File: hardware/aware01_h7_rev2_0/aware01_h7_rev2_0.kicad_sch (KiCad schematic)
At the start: 44 parts, among them J2 Conn_02x07_Odd_Even, J3 Conn_02x05_Odd_Even, SW1 SW_Push, U1 LMR50410Y5FQDBVRQ1, U2 STM32H7A3RITx, U7 LM1117MP-3.3, U8 LM4040DIM3X-10, Y2 WE-XTAL 24.0MHz 50ppm

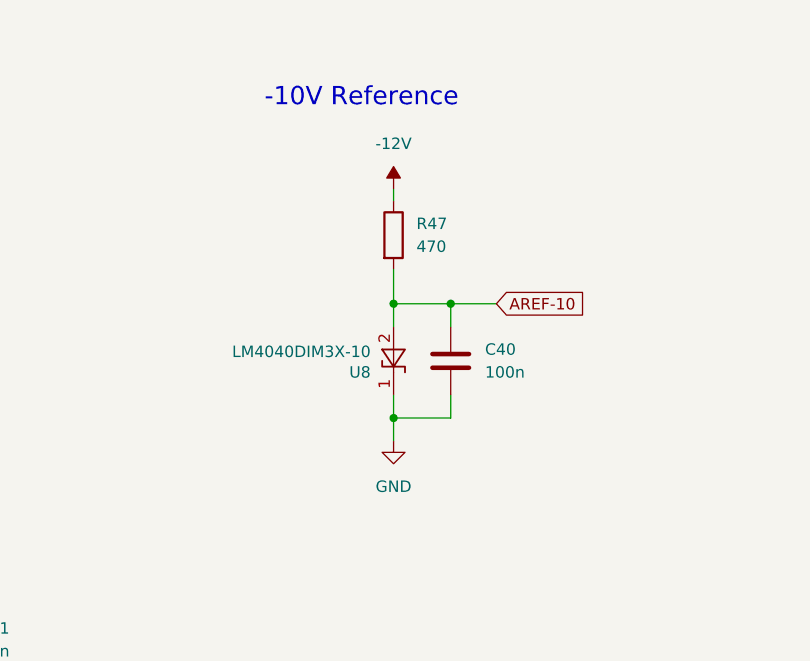
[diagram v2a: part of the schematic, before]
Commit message: refine layout, add testpoints
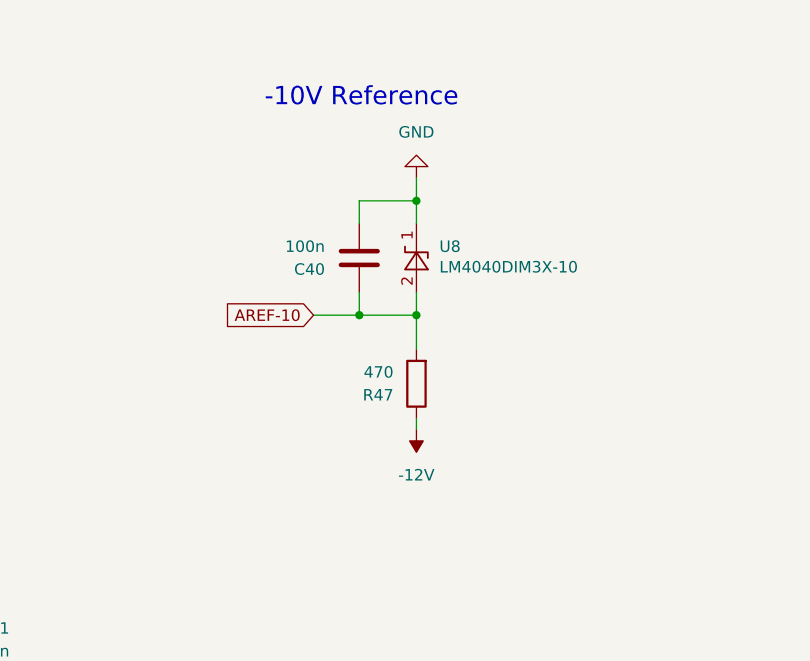
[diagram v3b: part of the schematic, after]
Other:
- moved on the sheet: C40, R47, U8
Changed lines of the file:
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@@
 	)
 	(junction
-		(at 274.32 57.15)
+		(at 276.86 58.42)
 		(diameter 0)
 		(color 0 0 0 0)
@@
 	)
 	(junction
-		(at 274.32 69.85)
+		(at 276.86 45.72)
 		(diameter 0)
 		(color 0 0 0 0)
@@
 	)
 	(junction
-		(at 280.67 57.15)
+		(at 270.51 58.42)
 		(diameter 0)
 		(color 0 0 0 0)
@@
 	(wire
 		(pts
-			(xy 274.32 44.45) (xy 274.32 45.72)
+			(xy 276.86 71.12) (xy 276.86 69.85)
 		)
 		(stroke
@@
 	(wire
 		(pts
-			(xy 274.32 53.34) (xy 274.32 57.15)
+			(xy 276.86 62.23) (xy 276.86 58.42)
 		)
 		(stroke
@@
 	(wire
 		(pts
-			(xy 280.67 57.15) (xy 285.75 57.15)
+			(xy 270.51 58.42) (xy 265.43 58.42)
 		)
 		(stroke
@@
 	(wire
 		(pts
-			(xy 280.67 57.15) (xy 280.67 59.69)
+			(xy 270.51 58.42) (xy 270.51 55.88)
 		)
 		(stroke
@@
 	(wire
 		(pts
-			(xy 280.67 67.31) (xy 280.67 69.85)
+			(xy 270.51 48.26) (xy 270.51 45.72)
 		)
 		(stroke
@@
 	(wire
 		(pts
-			(xy 280.67 69.85) (xy 274.32 69.85)
+			(xy 270.51 45.72) (xy 276.86 45.72)
 		)
 		(stroke
@@
 	(wire
 		(pts
-			(xy 274.32 57.15) (xy 280.67 57.15)
+			(xy 276.86 58.42) (xy 270.51 58.42)
 		)
 		(stroke
@@
 	(wire
 		(pts
-			(xy 274.32 69.85) (xy 274.32 72.39)
+			(xy 276.86 45.72) (xy 276.86 43.18)
 		)
 		(stroke
@@
 	(wire
 		(pts
-			(xy 274.32 67.31) (xy 274.32 69.85)
+			(xy 276.86 48.26) (xy 276.86 45.72)
 		)
 		(stroke
@@
 	(wire
 		(pts
-			(xy 274.32 57.15) (xy 274.32 59.69)
+			(xy 276.86 58.42) (xy 276.86 55.88)
 		)
 		(stroke
@@
 	(global_label "AREF-10"
 		(shape input)
-		(at 285.75 57.15 0)
+		(at 265.43 58.42 180)
 		(fields_autoplaced yes)
 		(effects
@@
 				(size 1.27 1.27)
 			)
-			(justify left)
+			(justify right)
 		)
 		(property "Intersheetrefs" "${INTERSHEET_REFS}"
-			(at 297.3228 57.15 0)
+			(at 253.8572 58.42 0)
 			(effects
 				(font
 					(size 1.27 1.27)
 				)
-				(justify left)
+				(justify right)
 				(hide yes)
 			)
@@
 	(symbol
 		(lib_id "power:GND")
-		(at 274.32 72.39 0)
+		(at 276.86 43.18 180)
 		(unit 1)
 		(exclude_from_sim no)
@@
 		(fields_autoplaced yes)
 		(property "Reference" "#PWR055"
-			(at 274.32 78.74 0)
+			(at 276.86 36.83 0)
 			(effects
 				(font
@@
 		)
 		(property "Value" "GND"
-			(at 274.32 77.47 0)
+			(at 276.86 38.1 0)
 			(effects
 				(font
@@
 		)
 		(property "Footprint" ""
-			(at 274.32 72.39 0)
+			(at 276.86 43.18 0)
 			(effects
 				(font
@@
 		)
 		(property "Datasheet" ""
-			(at 274.32 72.39 0)
+			(at 276.86 43.18 0)
 			(effects
 				(font
@@
 		)
 		(property "Description" "Power symbol creates a global label with name \"GND\" , ground"
-			(at 274.32 72.39 0)
+			(at 276.86 43.18 0)
 			(effects
 				(font
@@
 	(symbol
 		(lib_id "power:-12V")
-		(at 274.32 44.45 0)
+		(at 276.86 71.12 180)
 		(unit 1)
 		(exclude_from_sim no)
@@
 		(fields_autoplaced yes)
 		(property "Reference" "#PWR054"
-			(at 274.32 48.26 0)
+			(at 276.86 67.31 0)
 			(effects
 				(font
@@
 		)
 		(property "Value" "-12V"
-			(at 274.32 39.37 0)
+			(at 276.86 76.2 0)
 			(effects
 				(font
@@
 		)
 		(property "Footprint" ""
-			(at 274.32 44.45 0)
+			(at 276.86 71.12 0)
 			(effects
 				(font
@@
 		)
 		(property "Datasheet" ""
-			(at 274.32 44.45 0)
+			(at 276.86 71.12 0)
 			(effects
 				(font
@@
 		)
 		(property "Description" "Power symbol creates a global label with name \"-12V\""
-			(at 274.32 44.45 0)
+			(at 276.86 71.12 0)
 			(effects
 				(font
@@
 	(symbol
 		(lib_id "Device:C")
-		(at 280.67 63.5 0)
+		(at 270.51 52.07 180)
 		(unit 1)
 		(exclude_from_sim no)
@@
 		(fields_autoplaced yes)
 		(property "Reference" "C40"
-			(at 284.48 62.2299 0)
+			(at 266.7 53.3401 0)
 			(effects
 				(font
@@
 		)
 		(property "Value" "100n"
-			(at 284.48 64.7699 0)
+			(at 266.7 50.8001 0)
 			(effects
 				(font
@@
 		)
 		(property "Footprint" "Capacitor_SMD:C_0603_1608Metric"
-			(at 281.6352 67.31 0)
+			(at 269.5448 48.26 0)
 			(effects
 				(font
@@
 		)
 		(property "Datasheet" "~"
-			(at 280.67 63.5 0)
+			(at 270.51 52.07 0)
 			(effects
 				(font
@@
 		)
 		(property "Description" "Unpolarized capacitor"
-			(at 280.67 63.5 0)
+			(at 270.51 52.07 0)
 			(effects
 				(font
@@
 		)
 		(property "Manufacturer_Name" "KYOCERA AVX "
-			(at 280.67 63.5 0)
+			(at 270.51 52.07 0)
 			(effects
 				(font
@@
 		)
 		(property "Manufacturer_Part_Number" "KAF15BR72A104KT"
-			(at 280.67 63.5 0)
+			(at 270.51 52.07 0)
 			(effects
 				(font
@@
 		)
 		(property "Mouser Part Number" "581-KAF15BR72A104KT"
-			(at 280.67 63.5 0)
+			(at 270.51 52.07 0)
 			(effects
 				(font
@@
 	(symbol
 		(lib_id "Reference_Voltage:LM4040DBZ-10")
-		(at 274.32 63.5 270)
+		(at 276.86 52.07 90)
 		(unit 1)
 		(exclude_from_sim no)
@@
 		(dnp no)
 		(property "Reference" "U8"
-			(at 271.78 64.77 90)
+			(at 279.4 50.8 90)
 			(effects
 				(font
@@
 		)
 		(property "Value" "LM4040DIM3X-10"
-			(at 271.78 62.484 90)
+			(at 279.4 53.086 90)
 			(effects
 				(font
@@
 		)
 		(property "Footprint" "Package_TO_SOT_SMD:SOT-23"
-			(at 269.24 63.5 0)
+			(at 281.94 52.07 0)
 			(effects
 				(font
@@
 		)
 		(property "Datasheet" "http://www.ti.com/lit/ds/symlink/lm4040-n.pdf"
-			(at 274.32 63.5 0)
+			(at 276.86 52.07 0)
 			(effects
 				(font
@@
 		)
 		(property "Description" "10.00V Precision Micropower Shunt Voltage Reference, SOT-23"
-			(at 274.32 63.5 0)
+			(at 276.86 52.07 0)
 			(effects
 				(font
@@
 		)
 		(property "Manufacturer_Name" "Texas Instruments"
-			(at 274.32 63.5 0)
+			(at 276.86 52.07 0)
 			(effects
 				(font
@@
 		)
 		(property "Manufacturer_Part_Number" "LM4040DIM3X-10/NOPB"
-			(at 274.32 63.5 0)
+			(at 276.86 52.07 0)
 			(effects
 				(font
@@
 		)
 		(property "Mouser Part Number" " 926-LM4040DIM3X10NPB"
-			(at 274.32 63.5 0)
+			(at 276.86 52.07 0)
 			(effects
 				(font
@@
 	(symbol
 		(lib_id "Device:R")
-		(at 274.32 49.53 0)
+		(at 276.86 66.04 180)
 		(unit 1)
 		(exclude_from_sim no)
@@
 		(fields_autoplaced yes)
 		(property "Reference" "R47"
-			(at 276.86 48.2599 0)
+			(at 274.32 67.3101 0)
 			(effects
 				(font
@@
 		)
 		(property "Value" "470"
-			(at 276.86 50.7999 0)
+			(at 274.32 64.7701 0)
 			(effects
 				(font
@@
 		)
 		(property "Footprint" "Resistor_SMD:R_0603_1608Metric_Pad0.98x0.95mm_HandSolder"
-			(at 272.542 49.53 90)
+			(at 278.638 66.04 90)
 			(effects
 				(font
@@
 		)
 		(property "Datasheet" "~"
-			(at 274.32 49.53 0)
+			(at 276.86 66.04 0)
 			(effects
 				(font
@@
 		)
 		(property "Description" "Resistor"
-			(at 274.32 49.53 0)
+			(at 276.86 66.04 0)
 			(effects
 				(font
@@
 		)
 		(property "Manufacturer_Name" "YAGEO"
-			(at 274.32 49.53 0)
+			(at 276.86 66.04 0)
 			(effects
 				(font
@@
 		)
 		(property "Manufacturer_Part_Number" "RC0603FR-07470RP"
-			(at 274.32 49.53 0)
+			(at 276.86 66.04 0)
 			(effects
 				(font
@@
 		)
 		(property "Mouser Part Number" "603-RC0603FR-07470RP "
-			(at 274.32 49.53 0)
+			(at 276.86 66.04 0)
 			(effects
 				(font

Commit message: hw: update hw design
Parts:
- removed C4: 100n, Capacitor_SMD:C_0603_1608Metric, symbol Device:C
- removed SW1: SW_Push, Eurorack:TS046643BK100SMT, symbol Switch:SW_Push
- added R1: 10k, Resistor_SMD:R_0603_1608Metric_Pad0.98x0.95mm_HandSolder, symbol Device:R
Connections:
- net +3.3V: now also R1.1
- net NRST: now also R1.2

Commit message: hardware: update analog sim and routing (wip)
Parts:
- added C5, C9: 10u, Capacitor_SMD:C_0603_1608Metric, symbol Device:C
- added U3: LM1117MP-1.8, Package_TO_SOT_SMD:SOT-223-3_TabPin2, symbol Regulator_Linear:LM1117MP-1.8
- renumbered C18 to C1, C7 to C10, C38 to C11, C39 to C12, C25 to C13, C20 to C14, C21 to C15, C24 to C16, C12 to C17, C26 to C18, C1 to C19, C6 to C2, C10 to C20, C13 to C21, C29 to C22, C2 to C23, C14 to C24, C11 to C25, C40 to C26, C19 to C3, C30 to C4, C22 to C6, C23 to C7, C33 to C8, D3 to D1, D1 to D2, D2 to D3, J2 to J1, J3 to J2, L2 to L1, R46 to R1, R3 to R2, R2 to R3, R1 to R4, R80 to R5, R81 to R6, R47 to R7, U7 to U2, U2 to U4, U8 to U5, Y2 to Y1
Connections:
- net +3.3V: now also C5.1, U3.3 (VI)
- net GND: now also C5.2, C9.2, U3.1 (GND)
- new net +1V8: C9.1, U3.2 (VO)
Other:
- moved on the sheet: C4, C8, D1, R1, U2

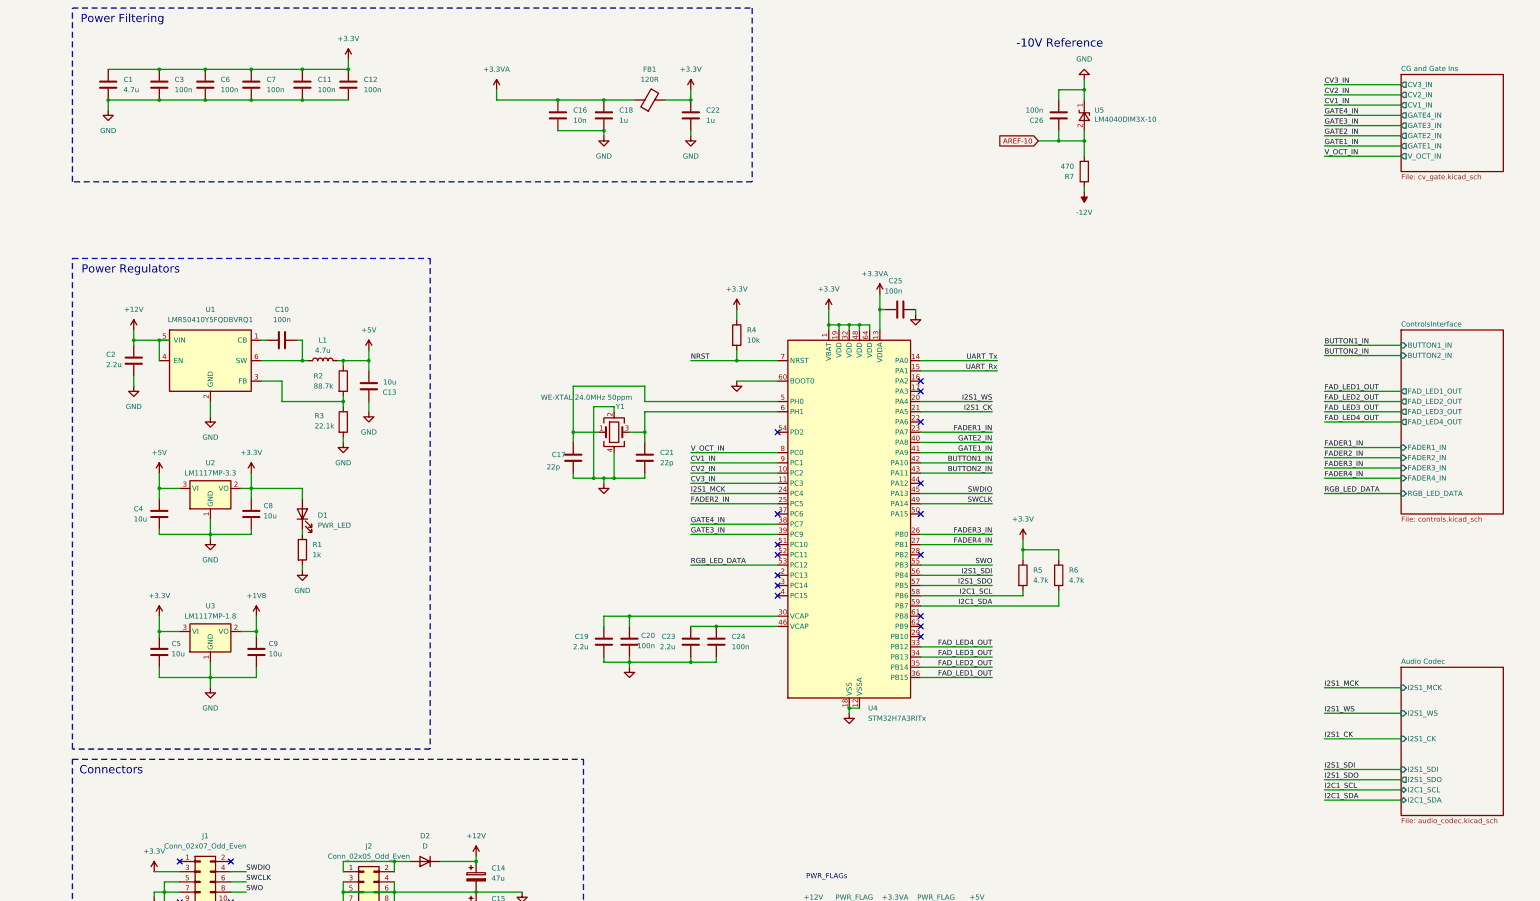
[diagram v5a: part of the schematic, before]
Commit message: hardware: update layout
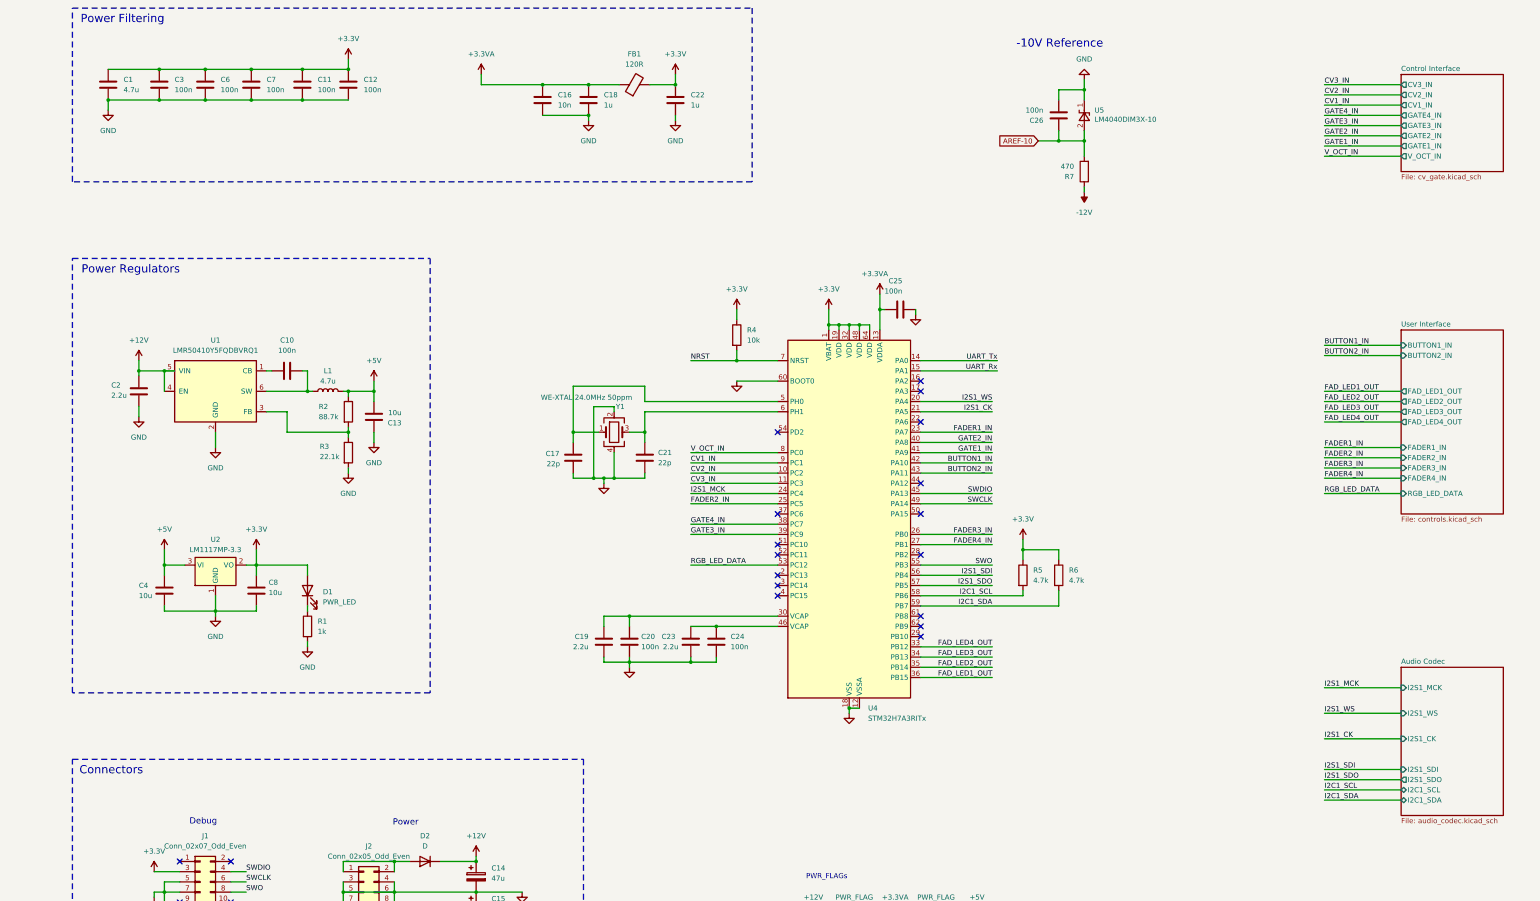
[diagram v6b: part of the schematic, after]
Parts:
- removed C5, C9: 10u, Capacitor_SMD:C_0603_1608Metric, symbol Device:C
- removed U3: LM1117MP-1.8, Package_TO_SOT_SMD:SOT-223-3_TabPin2, symbol Regulator_Linear:LM1117MP-1.8
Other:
- sheet CG and Gate Ins renamed Control Interface
- sheet ControlsInterface renamed User Interface
- note added: "Debug"
- note added: "Power"
- company: (none) -> Ausschussware
- title: (none) -> Aware 01 - Eurorack DSP Module
- moved on the sheet: C10, C13, C16, C18, C2, C22, C4, C8, D1, FB1, L1, R1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

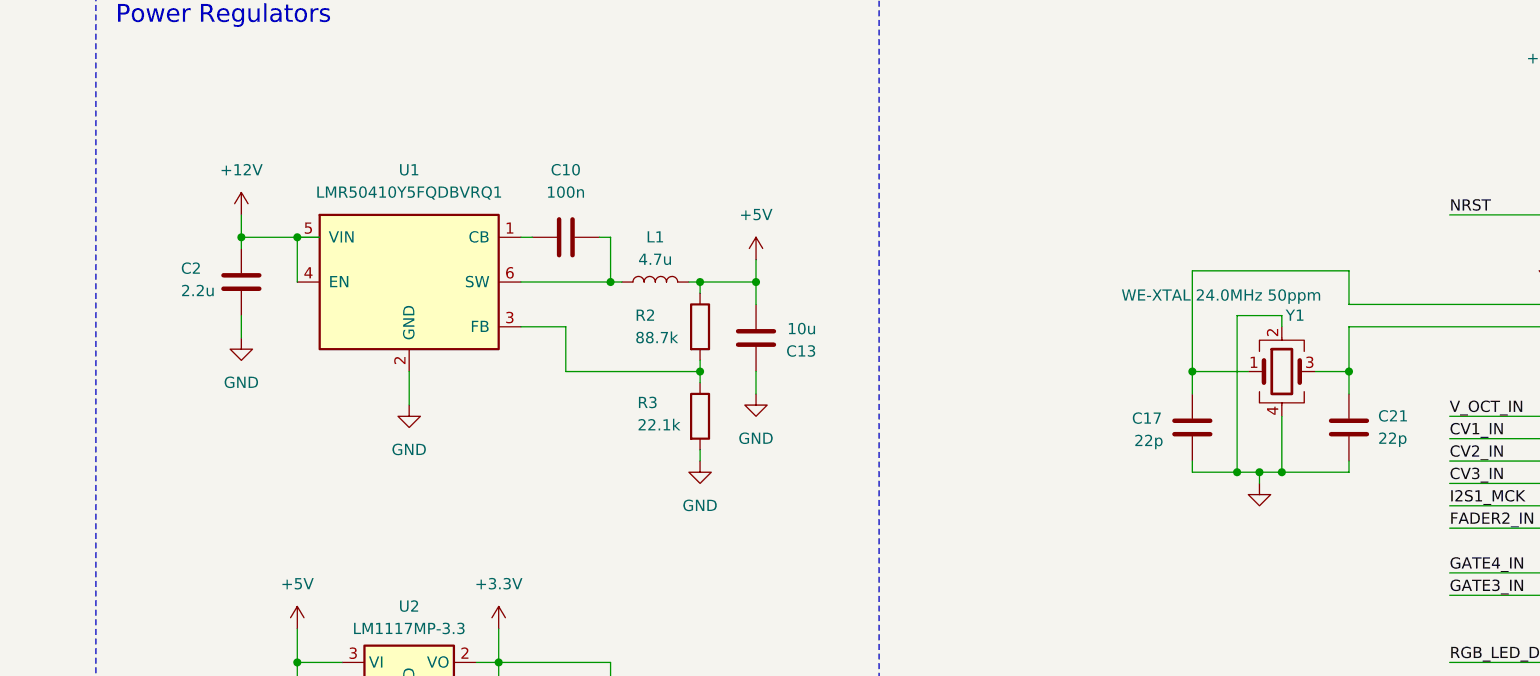
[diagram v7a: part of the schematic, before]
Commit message: hardware: adjust buck layout
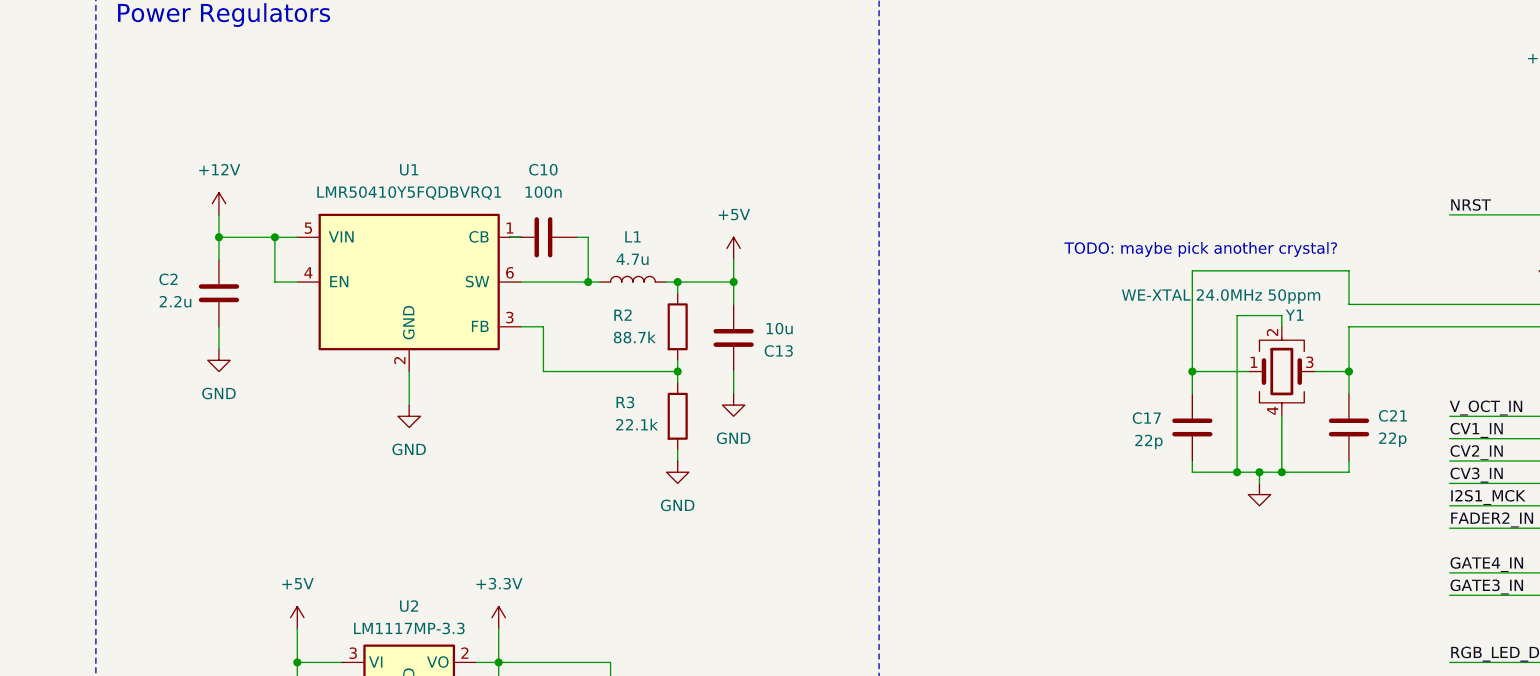
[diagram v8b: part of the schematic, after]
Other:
- note added: "TODO: maybe pick another crystal?"
- moved on the sheet: C10, C13, C2, L1, R2, R3
